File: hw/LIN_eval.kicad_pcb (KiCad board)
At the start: 2 copper layers, 43 x 30 mm, 68 parts, among them J1 STM32 SWD, J2 Conn_01x03, Q1 DMG1012T, Q2 DMG1012T, Q3 DMG1012T, Q4 DMG1012T, Q5 DMG1012T, Q6 DMG1012T, Q7 DMG1012T, U1 TJA1029TK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

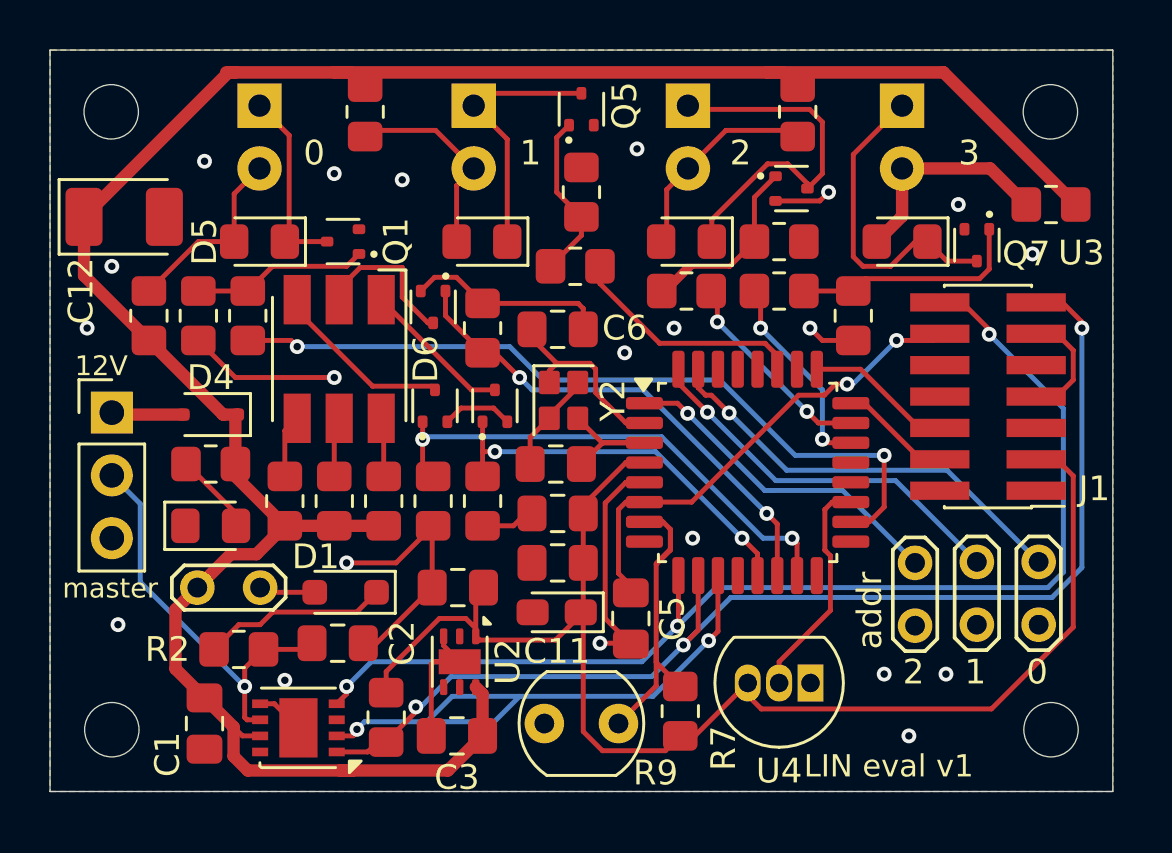
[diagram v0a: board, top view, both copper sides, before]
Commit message: hw: version v2 with improvements
- removed LIN UART RX/TX from debugger connector as it drives signal from two sources
- added 5k pull-up to DS18B20 1-Wire bus
- added 1.27mm connector for additional devices on 1-Wire bus
- shifted address jumpers little bit farther from debugger connector
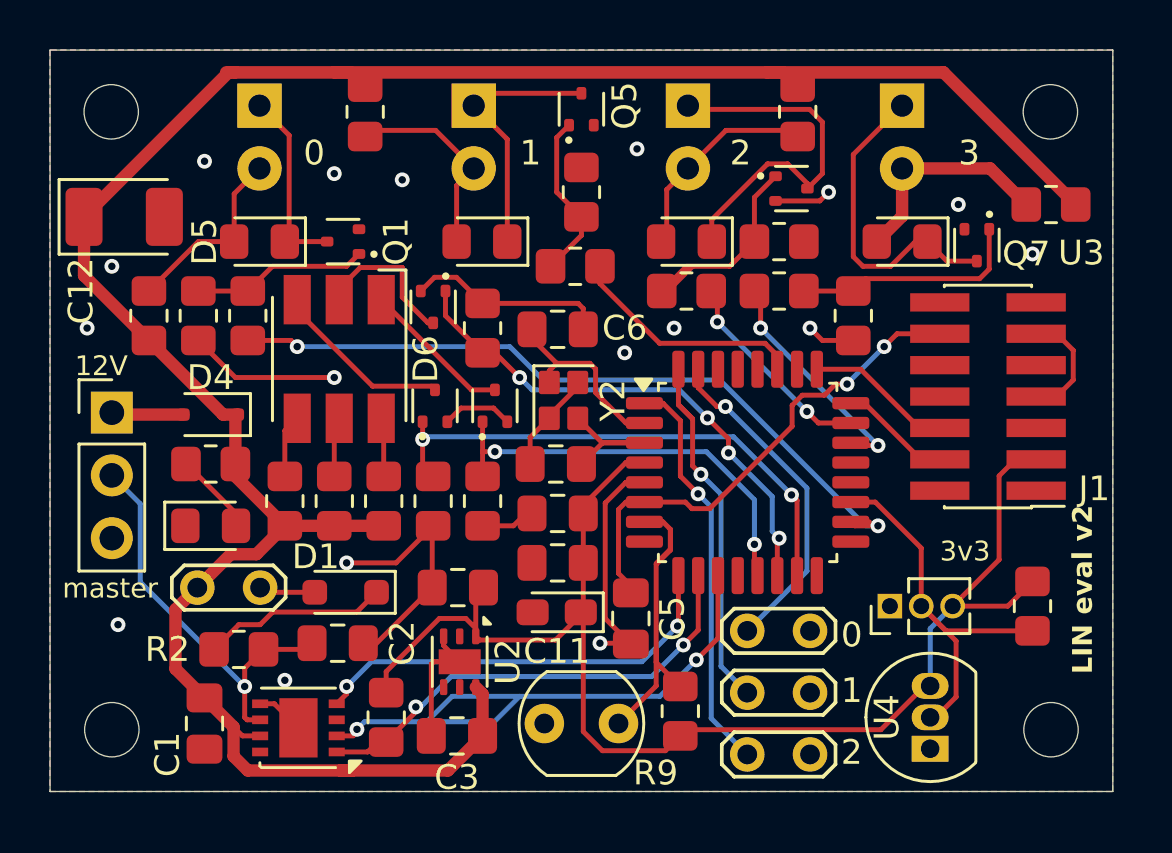
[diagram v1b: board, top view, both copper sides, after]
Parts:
- added J3: Conn_01x03, Connector_PinHeader_1.27mm:PinHeader_1x03_P1.27mm_Vertical, F.Cu at (154.0, 96.2)
- added R24: 5k, Resistor_SMD:R_0805_2012Metric_Pad1.20x1.40mm_HandSolder, F.Cu at (159.8, 96.2)
- moved JP4 9.25 mm to (150.8, 97.2), turned to 180 degrees
- moved JP3 7.29 mm to (150.8, 99.8), turned to 180 degrees
- moved JP2 6.72 mm to (150.8, 102.2), turned to 180 degrees
- moved U4 5.52 mm to (155.6, 102.0), turned to 90 degrees
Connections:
- J1 pad 13: /RXD -> unconnected-(J1-VCP_RX-Pad13)
- J1 pad 14: /TXD -> unconnected-(J1-VCP_TX-Pad14)
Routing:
- net /TXD: track 47.5 -> 17.4 mm, vias 3 -> 2
- net /RXD: track 49.1 -> 19.6 mm, vias 3 -> 2
- net Net-(J3-Pin_2): track 9.15 -> 16.5 mm
- net Net-(JP4-B): track 17.4 -> 13.6 mm
- net Net-(JP2-B): track 14.0 -> 16.4 mm
- net /LED_R: track 15.9 -> 17.1 mm
- net /LED_3: track 8.35 -> 9.47 mm
- net /LED_B: track 20.7 -> 21.7 mm
- net /LED_G: track 20.0 -> 20.9 mm, vias 2 -> 4
- net /LED_0: track 31.4 -> 30.5 mm
- net +3V3: track 56.7 -> 56.0 mm
- net /RST: track 19.2 -> 20.0 mm
- net Net-(JP3-B): track 15.6 -> 15.1 mm
- net GND: vias 21 -> 17
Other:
- board text added: "3v3"
- board text added: "LIN eval v2"
- board text removed: "LIN eval v1"
- board text removed: "addr"
